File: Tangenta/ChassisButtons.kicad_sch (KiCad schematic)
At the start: 19 parts, among them J2 Conn_02x02_Top_Bottom, Q1 2N7002, Q2 2N7002, U5 74HC74D,653, U6 CD4060SA_TR, U7 74HC04D,653

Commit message: Routing...
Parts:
- added C32, C33, C34: 100nF, Capacitor_SMD:C_0603_1608Metric, symbol Device:C_Small
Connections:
- net 5V_STANDBY: now also C32.1, C33.1, C34.1
- net GNDREF: now also C32.2, C33.2, C34.2
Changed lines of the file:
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@@
+    (stroke (width 0) (type default))
+  )
+  (wire (pts (xy 144.78 127.635) (xy 153.035 127.635))
     (stroke (width 0) (type default))
   )
@@
     (stroke (width 0) (type default))
   )
+  (wire (pts (xy 204.47 82.55) (xy 212.725 82.55))
+    (stroke (width 0) (type default))
+  )
   (wire (pts (xy 151.765 111.125) (xy 160.02 111.125))
     (stroke (width 0) (type default))
   )
+  (wire (pts (xy 217.805 82.55) (xy 226.06 82.55))
+    (stroke (width 0) (type default))
+  )
   (wire (pts (xy 252.73 58.42) (xy 252.73 78.74))
     (stroke (width 0) (type default))
@@
     (stroke (width 0) (type default))
   )
+  (wire (pts (xy 144.78 82.55) (xy 153.035 82.55))
+    (stroke (width 0) (type default))
+  )
   (wire (pts (xy 40.64 101.6) (xy 47.625 101.6))
     (stroke (width 0) (type default))
@@
     (stroke (width 0) (type default))
   )
+  (wire (pts (xy 131.445 127.635) (xy 139.7 127.635))
+    (stroke (width 0) (type default))
+  )
   (wire (pts (xy 42.545 55.88) (xy 67.945 55.88))
     (stroke (width 0) (type default))
@@
   )
   (wire (pts (xy 194.31 102.235) (xy 226.695 102.235))
+    (stroke (width 0) (type default))
+  )
+  (wire (pts (xy 131.445 82.55) (xy 139.7 82.55))
     (stroke (width 0) (type default))
   )
@@
     (effects (font (size 1.27 1.27)) (justify left bottom))
   )
+  (label "VCC_LOGIC" (at 131.445 82.55 0) (fields_autoplaced)
+    (effects (font (size 1.27 1.27)) (justify left bottom))
+  )
   (label "CONN_2" (at 121.285 66.04 0) (fields_autoplaced)
     (effects (font (size 1.27 1.27)) (justify left bottom))
@@
   )
   (label "VCC_LOGIC" (at 55.88 68.58 0) (fields_autoplaced)
+    (effects (font (size 1.27 1.27)) (justify left bottom))
+  )
+  (label "VCC_LOGIC" (at 131.445 127.635 0) (fields_autoplaced)
     (effects (font (size 1.27 1.27)) (justify left bottom))
   )
@@
     (effects (font (size 1.27 1.27)) (justify left bottom))
   )
+  (label "VCC_LOGIC" (at 204.47 82.55 0) (fields_autoplaced)
+    (effects (font (size 1.27 1.27)) (justify left bottom))
+  )
   (label "CONN_3" (at 153.035 108.585 0) (fields_autoplaced)
     (effects (font (size 1.27 1.27)) (justify left bottom))
@@
         (path "/358d1bcf-7599-4352-8c4d-baa18a5f09e6/8215796b-9611-4f43-bcc5-319f8414b8a6"
           (reference "#PWR09") (unit 1)
+        )
+      )
+    )
+  )
+  (symbol (lib_id "power:GNDREF") (at 153.035 127.635 0) (unit 1)
+    (in_bom yes) (on_board yes) (dnp no) (fields_autoplaced)
+    (property "Reference" "#PWR028" (at 153.035 133.985 0)
+      (effects (font (size 1.27 1.27)) hide)
+    )
+    (property "Value" "GNDREF" (at 153.035 132.715 0)
+      (effects (font (size 1.27 1.27)) hide)
+    )
+    (property "Footprint" "" (at 153.035 127.635 0)
+      (effects (font (size 1.27 1.27)) hide)
+    )
+    (property "Datasheet" "" (at 153.035 127.635 0)
+      (effects (font (size 1.27 1.27)) hide)
+    )
+    (pin "1")
+    (instances
+      (project "Tangenta"
+        (path "/358d1bcf-7599-4352-8c4d-baa18a5f09e6/8215796b-9611-4f43-bcc5-319f8414b8a6"
+          (reference "#PWR028") (unit 1)
         )
       )
@@
     )
   )
+  (symbol (lib_id "Device:C_Small") (at 142.24 82.55 90) (unit 1)
+    (in_bom yes) (on_board yes) (dnp no)
+    (property "Reference" "C32" (at 139.065 83.82 90)
+      (effects (font (size 1.27 1.27)))
+    )
+    (property "Value" "100nF" (at 146.685 83.82 90)
+      (effects (font (size 1.27 1.27)))
+    )
+    (property "Footprint" "Capacitor_SMD:C_0603_1608Metric" (at 142.24 82.55 0)
+      (effects (font (size 1.27 1.27)) hide)
+    )
+    (property "Datasheet" "~" (at 142.24 82.55 0)
+      (effects (font (size 1.27 1.27)) hide)
+    )
+    (pin "1")
+    (pin "2")
+    (instances
+      (project "Tangenta"
+        (path "/358d1bcf-7599-4352-8c4d-baa18a5f09e6/8215796b-9611-4f43-bcc5-319f8414b8a6"
+          (reference "C32") (unit 1)
+        )
+      )
+    )
+  )
+  (symbol (lib_id "power:GNDREF") (at 226.06 82.55 0) (unit 1)
+    (in_bom yes) (on_board yes) (dnp no) (fields_autoplaced)
+    (property "Reference" "#PWR027" (at 226.06 88.9 0)
+      (effects (font (size 1.27 1.27)) hide)
+    )
+    (property "Value" "GNDREF" (at 226.06 87.63 0)
+      (effects (font (size 1.27 1.27)) hide)
+    )
+    (property "Footprint" "" (at 226.06 82.55 0)
+      (effects (font (size 1.27 1.27)) hide)
+    )
+    (property "Datasheet" "" (at 226.06 82.55 0)
+      (effects (font (size 1.27 1.27)) hide)
+    )
+    (pin "1")
+    (instances
+      (project "Tangenta"
+        (path "/358d1bcf-7599-4352-8c4d-baa18a5f09e6/8215796b-9611-4f43-bcc5-319f8414b8a6"
+          (reference "#PWR027") (unit 1)
+        )
+      )
+    )
+  )
+  (symbol (lib_id "power:GNDREF") (at 153.035 82.55 0) (unit 1)
+    (in_bom yes) (on_board yes) (dnp no) (fields_autoplaced)
+    (property "Reference" "#PWR026" (at 153.035 88.9 0)
+      (effects (font (size 1.27 1.27)) hide)
+    )
+    (property "Value" "GNDREF" (at 153.035 87.63 0)
+      (effects (font (size 1.27 1.27)) hide)
+    )
+    (property "Footprint" "" (at 153.035 82.55 0)
+      (effects (font (size 1.27 1.27)) hide)
+    )
+    (property "Datasheet" "" (at 153.035 82.55 0)
+      (effects (font (size 1.27 1.27)) hide)
+    )
+    (pin "1")
+    (instances
+      (project "Tangenta"
+        (path "/358d1bcf-7599-4352-8c4d-baa18a5f09e6/8215796b-9611-4f43-bcc5-319f8414b8a6"
+          (reference "#PWR026") (unit 1)
+        )
+      )
+    )
+  )
   (symbol (lib_id "Device:R_Small_US") (at 168.275 116.205 90) (unit 1)
     (in_bom yes) (on_board yes) (dnp no)
@@
         (path "/358d1bcf-7599-4352-8c4d-baa18a5f09e6/8215796b-9611-4f43-bcc5-319f8414b8a6"
           (reference "R3") (unit 1)
+        )
+      )
+    )
+  )
+  (symbol (lib_id "Device:C_Small") (at 215.265 82.55 90) (unit 1)
+    (in_bom yes) (on_board yes) (dnp no)
+    (property "Reference" "C33" (at 212.09 83.82 90)
+      (effects (font (size 1.27 1.27)))
+    )
+    (property "Value" "100nF" (at 219.71 83.82 90)
+      (effects (font (size 1.27 1.27)))
+    )
+    (property "Footprint" "Capacitor_SMD:C_0603_1608Metric" (at 215.265 82.55 0)
+      (effects (font (size 1.27 1.27)) hide)
+    )
+    (property "Datasheet" "~" (at 215.265 82.55 0)
+      (effects (font (size 1.27 1.27)) hide)
+    )
+    (pin "1")
+    (pin "2")
+    (instances
+      (project "Tangenta"
+        (path "/358d1bcf-7599-4352-8c4d-baa18a5f09e6/8215796b-9611-4f43-bcc5-319f8414b8a6"
+          (reference "C33") (unit 1)
         )
       )
@@
         )
       )
+    )
+  )
+  (symbol (lib_id "Device:C_Small") (at 142.24 127.635 90) (unit 1)
+    (in_bom yes) (on_board yes) (dnp no)
+    (property "Reference" "C34" (at 139.065 128.905 90)
+      (effects (font (size 1.27 1.27)))
+    )
+    (property "Value" "100nF" (at 146.05 128.905 90)
+      (effects (font (size 1.27 1.27)))
+    )
+    (property "Footprint" "Capacitor_SMD:C_0603_1608Metric" (at 142.24 127.635 0)
+      (effects (font (size 1.27 1.27)) hide)
+    )
+    (property "Datasheet" "~" (at 142.24 127.635 0)
+      (effects (font (size 1.27 1.27)) hide)
+    )
+    (pin "1")
+    (pin "2")
+    (instances
+      (project "Tangenta"
+        (path "/358d1bcf-7599-4352-8c4d-baa18a5f09e6/8215796b-9611-4f43-bcc5-319f8414b8a6"
+          (reference "C34") (unit 1)
+        )
+      )

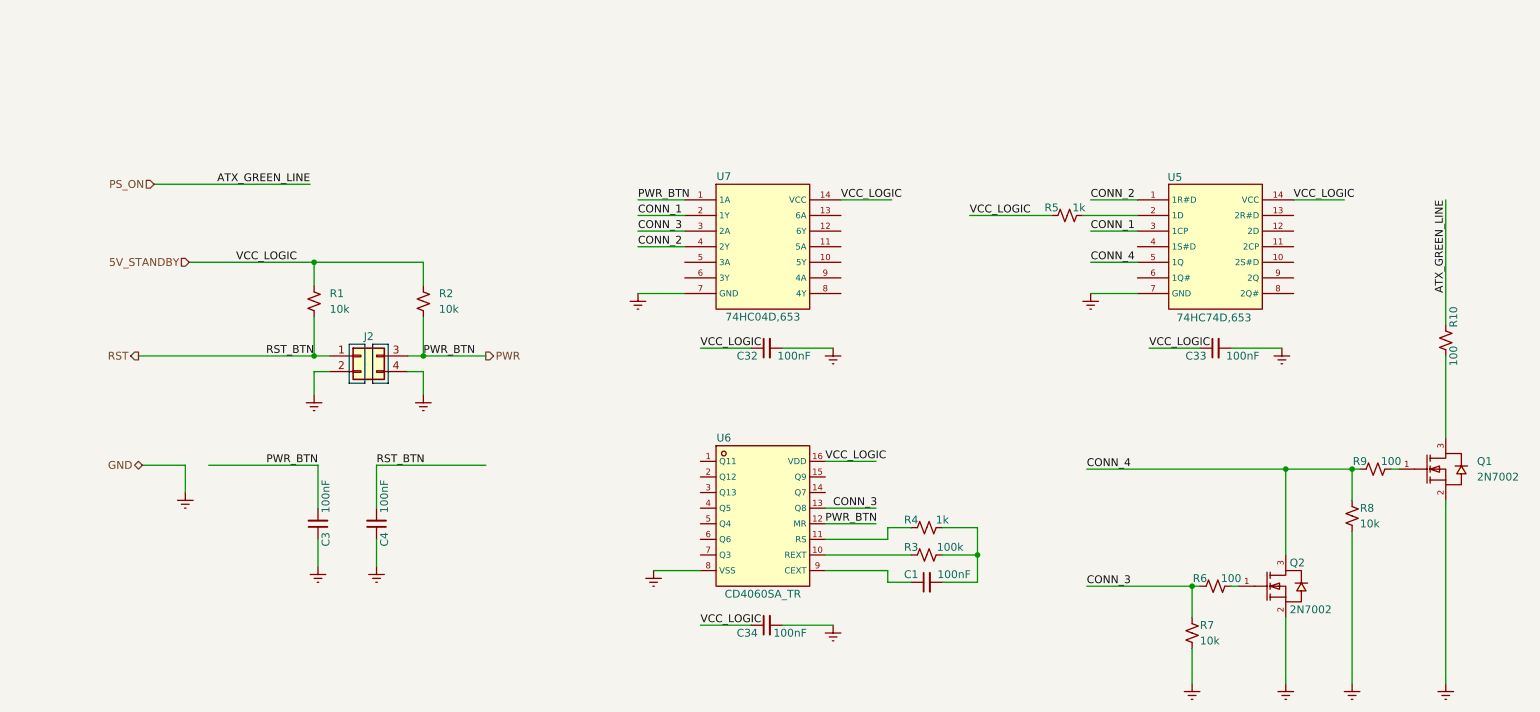
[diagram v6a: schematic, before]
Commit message: PCIe at Toradex side; handling unconnected pins.
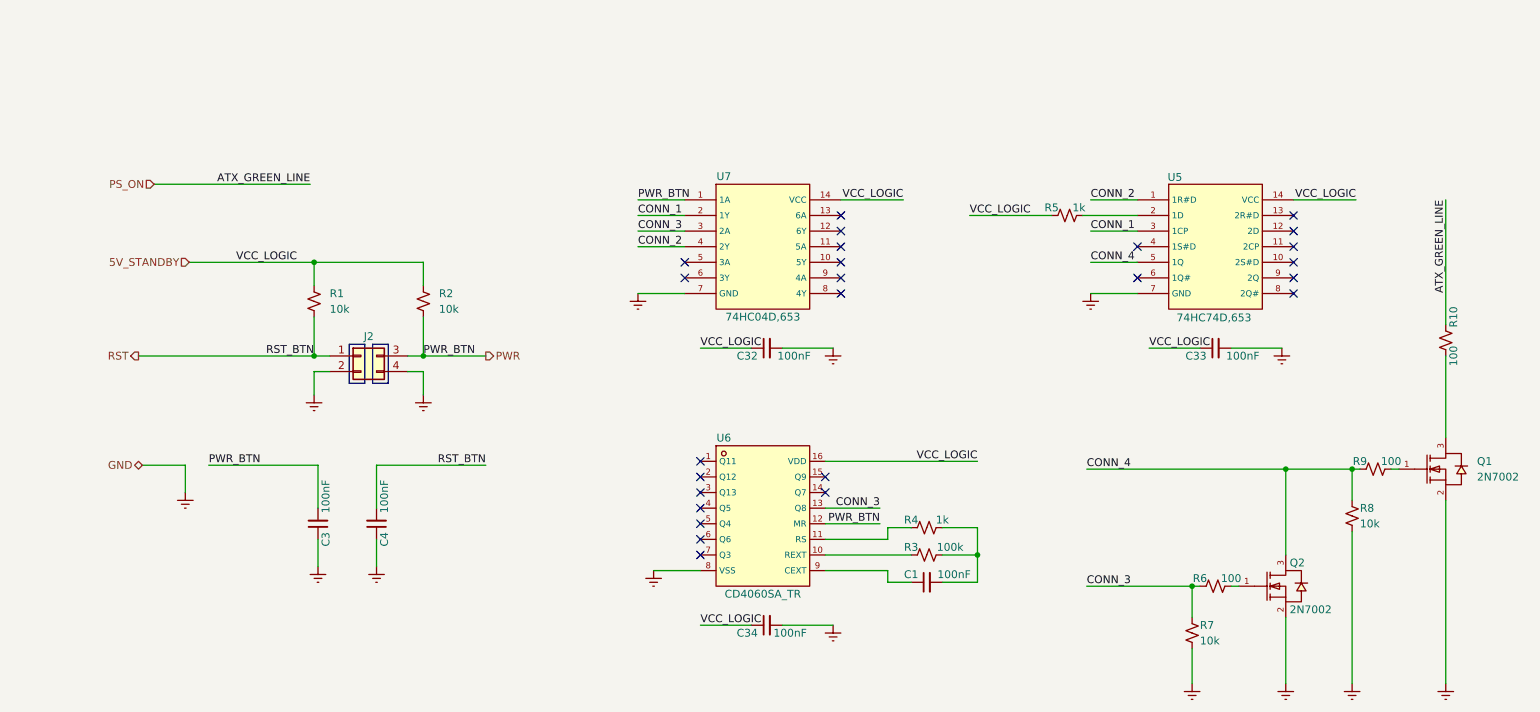
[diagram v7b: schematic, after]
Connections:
- no-connect marks 0 -> 25
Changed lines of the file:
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@@
   (junction (at 68.58 83.82) (diameter 0) (color 0 0 0 0)
   )
+  (no_connect (at 154.305 71.12))
+  (no_connect (at 131.445 113.665))
+  (no_connect (at 154.305 73.66))
+  (no_connect (at 202.565 71.12))
+  (no_connect (at 128.905 68.58))
+  (no_connect (at 131.445 116.205))
+  (no_connect (at 131.445 106.045))
+  (no_connect (at 154.305 66.04))
+  (no_connect (at 131.445 100.965))
+  (no_connect (at 151.765 106.045))
+  (no_connect (at 151.765 103.505))
+  (no_connect (at 131.445 103.505))
+  (no_connect (at 154.305 68.58))
+  (no_connect (at 227.965 71.12))
+  (no_connect (at 131.445 108.585))
+  (no_connect (at 128.905 71.12))
+  (no_connect (at 227.965 73.66))
+  (no_connect (at 227.965 68.58))
+  (no_connect (at 202.565 66.04))
+  (no_connect (at 131.445 111.125))
+  (no_connect (at 227.965 63.5))
+  (no_connect (at 227.965 60.96))
+  (no_connect (at 227.965 66.04))
+  (no_connect (at 154.305 63.5))
+  (no_connect (at 154.305 60.96))
   (wire (pts (xy 68.58 86.36) (xy 71.12 86.36))
     (stroke (width 0) (type default))
@@
     (stroke (width 0) (type default))
   )
-  (wire (pts (xy 151.765 100.965) (xy 160.02 100.965))
+  (wire (pts (xy 151.765 100.965) (xy 176.53 100.965))
     (stroke (width 0) (type default))
   )
@@
     (stroke (width 0) (type default))
   )
-  (wire (pts (xy 151.765 111.125) (xy 160.02 111.125))
+  (wire (pts (xy 151.765 111.125) (xy 160.655 111.125))
     (stroke (width 0) (type default))
   )
@@
     (stroke (width 0) (type default))
   )
-  (wire (pts (xy 151.765 108.585) (xy 160.02 108.585))
+  (wire (pts (xy 151.765 108.585) (xy 160.655 108.585))
     (stroke (width 0) (type default))
   )
@@
     (stroke (width 0) (type default))
   )
-  (wire (pts (xy 227.965 58.42) (xy 236.22 58.42))
+  (wire (pts (xy 227.965 58.42) (xy 238.125 58.42))
     (stroke (width 0) (type default))
   )
@@
     (stroke (width 0) (type default))
   )
-  (wire (pts (xy 154.305 58.42) (xy 162.56 58.42))
+  (wire (pts (xy 154.305 58.42) (xy 164.465 58.42))
     (stroke (width 0) (type default))
   )
@@
     (effects (font (size 1.27 1.27)) (justify left bottom))
   )
-  (label "VCC_LOGIC" (at 154.305 58.42 0) (fields_autoplaced)
-    (effects (font (size 1.27 1.27)) (justify left bottom))
+  (label "VCC_LOGIC" (at 164.465 58.42 180) (fields_autoplaced)
+    (effects (font (size 1.27 1.27)) (justify right bottom))
   )
   (label "CONN_3" (at 121.285 63.5 0) (fields_autoplaced)
     (effects (font (size 1.27 1.27)) (justify left bottom))
   )
-  (label "RST_BTN" (at 78.74 101.6 0) (fields_autoplaced)
-    (effects (font (size 1.27 1.27)) (justify left bottom))
+  (label "RST_BTN" (at 96.52 101.6 180) (fields_autoplaced)
+    (effects (font (size 1.27 1.27)) (justify right bottom))
   )
   (label "ATX_GREEN_LINE" (at 252.73 58.42 270) (fields_autoplaced)
     (effects (font (size 1.27 1.27)) (justify right bottom))
   )
-  (label "PWR_BTN" (at 151.765 111.125 0) (fields_autoplaced)
-    (effects (font (size 1.27 1.27)) (justify left bottom))
-  )
-  (label "VCC_LOGIC" (at 227.965 58.42 0) (fields_autoplaced)
-    (effects (font (size 1.27 1.27)) (justify left bottom))
+  (label "PWR_BTN" (at 160.655 111.125 180) (fields_autoplaced)
+    (effects (font (size 1.27 1.27)) (justify right bottom))
+  )
+  (label "VCC_LOGIC" (at 238.125 58.42 180) (fields_autoplaced)
+    (effects (font (size 1.27 1.27)) (justify right bottom))
   )
   (label "RST_BTN" (at 68.58 83.82 180) (fields_autoplaced)
@@
     (effects (font (size 1.27 1.27)) (justify left bottom))
   )
-  (label "VCC_LOGIC" (at 151.765 100.965 0) (fields_autoplaced)
-    (effects (font (size 1.27 1.27)) (justify left bottom))
+  (label "VCC_LOGIC" (at 176.53 100.965 180) (fields_autoplaced)
+    (effects (font (size 1.27 1.27)) (justify right bottom))
   )
   (label "VCC_LOGIC" (at 55.88 68.58 0) (fields_autoplaced)
@@
     (effects (font (size 1.27 1.27)) (justify right bottom))
   )
-  (label "PWR_BTN" (at 69.215 101.6 180) (fields_autoplaced)
-    (effects (font (size 1.27 1.27)) (justify right bottom))
+  (label "PWR_BTN" (at 51.435 101.6 0) (fields_autoplaced)
+    (effects (font (size 1.27 1.27)) (justify left bottom))
   )
   (label "CONN_4" (at 194.31 102.235 0) (fields_autoplaced)
@@
     (effects (font (size 1.27 1.27)) (justify left bottom))
   )
-  (label "CONN_3" (at 153.035 108.585 0) (fields_autoplaced)
-    (effects (font (size 1.27 1.27)) (justify left bottom))
+  (label "CONN_3" (at 160.655 108.585 180) (fields_autoplaced)
+    (effects (font (size 1.27 1.27)) (justify right bottom))
   )
   (label "CONN_1" (at 121.285 60.96 0) (fields_autoplaced)
